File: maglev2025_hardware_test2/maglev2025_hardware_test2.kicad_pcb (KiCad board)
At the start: 4 copper layers, 100 x 100 mm, 106 parts, among them J1 SWD, J2 PWRIn, U1 RY8411, U10 INA240A1PW, U11 INA240A1PW, U12 INA240A1PW, U2 TMAG5170-Q1, U3 STM32G474RBTx, U4 RS3236, U5 AT8236, U6 AT8236, U7 AT8236, U8 AT8236, U9 INA240A1PW, Y1 25MHz

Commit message: finish test2 sche
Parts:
- added C54: 100n, Capacitor_SMD:C_0603_1608Metric, F.Cu at (-25.0, 69.7)
- added C55: 100n, Capacitor_SMD:C_0603_1608Metric, F.Cu at (-25.0, 72.2)
- added C56: 100n, Capacitor_SMD:C_0603_1608Metric, F.Cu at (-25.0, 74.7)
- added C57: 10n, Capacitor_SMD:C_0603_1608Metric, F.Cu at (-25.0, 77.2)
- added C58: 100u 16V, Capacitor_THT:CP_Radial_D6.3mm_P2.50mm, F.Cu at (-42.2, 72.3)
- added C59: 10u, Capacitor_SMD:C_1206_3216Metric, F.Cu at (-42.2, 100.8)
- added C60: 100n, Capacitor_SMD:C_0603_1608Metric, F.Cu at (-43.0, 85.4)
- added C61: 10n, Capacitor_SMD:C_0603_1608Metric, F.Cu at (-43.0, 87.9)
- added C62: 100u 16V, Capacitor_THT:CP_Radial_D6.3mm_P2.50mm, F.Cu at (-42.2, 80.2)
- added C63: 10u, Capacitor_SMD:C_1206_3216Metric, F.Cu at (-42.2, 104.2)
- added C64: 10u, Capacitor_SMD:C_1206_3216Metric, F.Cu at (-42.2, 107.5)
- added C65: 10u, Capacitor_SMD:C_0603_1608Metric, F.Cu at (-43.0, 90.4)
- added C66: 20p, Capacitor_SMD:C_0603_1608Metric, F.Cu at (-43.0, 92.9)
- added C67: 100n, Capacitor_SMD:C_0603_1608Metric, F.Cu at (-43.0, 95.4)
- added C68: 100n, Capacitor_SMD:C_0603_1608Metric, F.Cu at (-43.0, 97.9)
- added C69: 100n, Capacitor_SMD:C_0603_1608Metric, F.Cu at (-39.0, 85.4)
- added C70: 100n, Capacitor_SMD:C_0603_1608Metric, F.Cu at (-39.0, 87.9)
- added C71: 100n, Capacitor_SMD:C_0603_1608Metric, F.Cu at (-39.0, 90.4)
- added C72: 100n, Capacitor_SMD:C_0603_1608Metric, F.Cu at (-39.0, 92.9)
- added C73: 100n, Capacitor_SMD:C_0603_1608Metric, F.Cu at (-39.0, 95.4)
- added C74: 100n, Capacitor_SMD:C_0603_1608Metric, F.Cu at (-39.0, 97.9)
- added C75: 100n, Capacitor_SMD:C_0603_1608Metric, F.Cu at (-35.0, 85.4)
- added C76: 100n, Capacitor_SMD:C_0603_1608Metric, F.Cu at (-35.0, 87.9)
- added C77: 100n, Capacitor_SMD:C_0603_1608Metric, F.Cu at (-35.0, 90.4)
- added C78: 100n, Capacitor_SMD:C_0603_1608Metric, F.Cu at (-35.0, 92.9)
- added C79: 100n, Capacitor_SMD:C_0603_1608Metric, F.Cu at (-35.0, 95.4)
- added C80: 100n, Capacitor_SMD:C_0603_1608Metric, F.Cu at (-35.0, 97.9)
- added C81: 100n, Capacitor_SMD:C_0603_1608Metric, F.Cu at (-31.0, 85.4)
- added C82: 100n, Capacitor_SMD:C_0603_1608Metric, F.Cu at (-25.0, 79.7)
- added C83: 100n, Capacitor_SMD:C_0603_1608Metric, F.Cu at (-25.0, 82.2)
- added C84: 100n, Capacitor_SMD:C_0603_1608Metric, F.Cu at (-25.0, 84.7)
- added D10: WS2812B, LED_SMD:LED_WS2812B_PLCC4_5.0x5.0mm_P3.2mm, F.Cu at (-65.3, 98.2)
- added D11: DSS34, Diode_SMD:D_SMF, F.Cu at (-36.5, 107.5)
- added D12: WS2812B, LED_SMD:LED_WS2812B_PLCC4_5.0x5.0mm_P3.2mm, F.Cu at (-65.3, 104.8)
- added D13: WS2812B, LED_SMD:LED_WS2812B_PLCC4_5.0x5.0mm_P3.2mm, F.Cu at (-57.2, 71.7)
- added D14: WS2812B, LED_SMD:LED_WS2812B_PLCC4_5.0x5.0mm_P3.2mm, F.Cu at (-57.2, 78.3)
- added D15: WS2812B, LED_SMD:LED_WS2812B_PLCC4_5.0x5.0mm_P3.2mm, F.Cu at (-57.2, 85.0)
- added D16: WS2812B, LED_SMD:LED_WS2812B_PLCC4_5.0x5.0mm_P3.2mm, F.Cu at (-57.2, 91.6)
- added D17: WS2812B, LED_SMD:LED_WS2812B_PLCC4_5.0x5.0mm_P3.2mm, F.Cu at (-57.2, 98.2)
- added D18: WS2812B, LED_SMD:LED_WS2812B_PLCC4_5.0x5.0mm_P3.2mm, F.Cu at (-57.2, 104.8)
- added D19: WS2812B, LED_SMD:LED_WS2812B_PLCC4_5.0x5.0mm_P3.2mm, F.Cu at (-49.1, 71.7)
- added D20: WS2812B, LED_SMD:LED_WS2812B_PLCC4_5.0x5.0mm_P3.2mm, F.Cu at (-49.1, 78.3)
- added D21: WS2812B, LED_SMD:LED_WS2812B_PLCC4_5.0x5.0mm_P3.2mm, F.Cu at (-49.1, 85.0)
- added D29: LED, LED_SMD:LED_0603_1608Metric, F.Cu at (0.41, 69.7)
- added D30: LED, LED_SMD:LED_0603_1608Metric, F.Cu at (0.41, 72.3)
- added D31: LED, LED_SMD:LED_0603_1608Metric, F.Cu at (0.41, 74.9)
- added D4: DSS34, Diode_SMD:D_SMA, F.Cu at (-22.9, 95.7)
- added D6: WS2812B, LED_SMD:LED_WS2812B_PLCC4_5.0x5.0mm_P3.2mm, F.Cu at (-65.3, 71.7)
- added D7: WS2812B, LED_SMD:LED_WS2812B_PLCC4_5.0x5.0mm_P3.2mm, F.Cu at (-65.3, 78.3)
- added D8: WS2812B, LED_SMD:LED_WS2812B_PLCC4_5.0x5.0mm_P3.2mm, F.Cu at (-65.3, 85.0)
- added D9: WS2812B, LED_SMD:LED_WS2812B_PLCC4_5.0x5.0mm_P3.2mm, F.Cu at (-65.3, 91.6)
- added F3: 5A, Fuse:Fuse_1206_3216Metric, F.Cu at (-15.5, 90.1)
- added J3: Conn_01x04, Connector_PinHeader_2.54mm:PinHeader_1x04_P2.54mm_Vertical, F.Cu at (-8.62, 70.7)
- added J4: Conn_01x04_MountingPin, Connector_JST:JST_GH_BM04B-GHS-TBT_1x04-1MP_P1.25mm_Vertical, F.Cu at (-5.70, 95.0)
- added J5: USB_C_Receptacle_USB2.0, Connector_USB:USB_C_Receptacle_HRO_TYPE-C-31-M-12, F.Cu at (-5.09, 86.5)
- added J6: Conn_01x04, Connector_PinHeader_2.54mm:PinHeader_1x04_P2.54mm_Vertical, F.Cu at (-3.96, 70.7)
- added L6: 15u, Inductor_SMD:L_Sunlord_MWSA0402S, F.Cu at (-33.7, 71.3)
- added Q1: AO3400A, Package_TO_SOT_SMD:SOT-23, F.Cu at (-34.6, 81.4)
- added R21: 33r, Resistor_SMD:R_0603_1608Metric, F.Cu at (-25.0, 87.2)
- added R22: 33r, Resistor_SMD:R_0603_1608Metric, F.Cu at (-21.0, 69.7)
- added R23: 4.7k, Resistor_SMD:R_0603_1608Metric, F.Cu at (-21.0, 72.2)
- added R24: 4.7k, Resistor_SMD:R_0603_1608Metric, F.Cu at (-21.0, 74.7)
- added R25: 33r, Resistor_SMD:R_0603_1608Metric, F.Cu at (-21.0, 77.2)
- added R26: 33r, Resistor_SMD:R_0603_1608Metric, F.Cu at (-21.0, 79.7)
- added R27: 1M, Resistor_SMD:R_0603_1608Metric, F.Cu at (-21.0, 82.2)
- added R28: 33r, Resistor_SMD:R_0603_1608Metric, F.Cu at (-21.0, 84.7)
- added R29: 33r, Resistor_SMD:R_0603_1608Metric, F.Cu at (-21.0, 87.2)
- added R30: R_US, Resistor_SMD:R_2512_6332Metric, F.Cu at (-22.6, 90.9)
- added R31: 10k, Resistor_SMD:R_0603_1608Metric, F.Cu at (-17.0, 69.7)
- added R32: 1k, Resistor_SMD:R_0603_1608Metric, F.Cu at (-17.0, 72.2)
- added R33: 3.24k, Resistor_SMD:R_0603_1608Metric, F.Cu at (-31.0, 90.4)
- added R34: 10k, Resistor_SMD:R_0603_1608Metric, F.Cu at (-31.0, 92.9)
- added R35: 33r, Resistor_SMD:R_0603_1608Metric, F.Cu at (-31.0, 95.4)
- added R36: 33R, Resistor_SMD:R_0603_1608Metric, F.Cu at (-31.0, 97.9)
- added R37: 33r, Resistor_SMD:R_0603_1608Metric, F.Cu at (-17.0, 74.7)
- added R38: 33r, Resistor_SMD:R_0603_1608Metric, F.Cu at (-17.0, 77.2)
- added R39: 33r, Resistor_SMD:R_0603_1608Metric, F.Cu at (-17.0, 79.7)
- added R40: 33r, Resistor_SMD:R_0603_1608Metric, F.Cu at (-17.0, 82.2)
- added R41: 330, Resistor_SMD:R_0603_1608Metric, F.Cu at (-17.0, 84.7)
- added R42: 1k, Resistor_SMD:R_0603_1608Metric, F.Cu at (-17.0, 87.2)
- added R43: 10k, Resistor_SMD:R_0603_1608Metric, F.Cu at (-12.9, 69.7)
- added R44: 330, Resistor_SMD:R_0603_1608Metric, F.Cu at (-12.9, 72.2)
- added R45: 1k, Resistor_SMD:R_0603_1608Metric, F.Cu at (-12.9, 74.7)
- added R46: 10k, Resistor_SMD:R_0603_1608Metric, F.Cu at (-12.9, 77.2)
- added R47: 330, Resistor_SMD:R_0603_1608Metric, F.Cu at (-12.9, 79.7)
- added R48: 1k, Resistor_SMD:R_0603_1608Metric, F.Cu at (-12.9, 82.2)
- added R49: 10k, Resistor_SMD:R_0603_1608Metric, F.Cu at (-12.9, 84.7)
- added R6: 10k, Resistor_SMD:R_0603_1608Metric, F.Cu at (-31.0, 87.9)
- added RN4: 33x4, Resistor_SMD:R_Array_Convex_4x0603, F.Cu at (-35.0, 76.6)
- added U13: TPS5430DDA, Package_SO:TI_SO-PowerPAD-8_ThermalVias, F.Cu at (-35.1, 102.6)
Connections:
- C1 pad 1: VREF -> VREF_MCU
- C2 pad 1: VREF -> VREF_MCU
- R11 pad 1: GND -> GND_PWR
- R12 pad 1: GND -> GND_PWR
- R13 pad 1: GND -> GND_PWR
- R14 pad 1: GND -> GND_PWR
- R20 pad 1: Net-(U3-PA15) -> Net-(U3-PA13)
- R4 pad 1: Net-(U3-PB7) -> Net-(U3-PA3)
- U3 pad 10: unconnected-(U3-PC2-Pad10) -> ISENSE_D_MCU
- U3 pad 11: unconnected-(U3-PC3-Pad11) -> ISENSE_C_MCU
- U3 pad 12: unconnected-(U3-PA0-Pad12) -> ISENSE_B_MCU
- U3 pad 13: unconnected-(U3-PA1-Pad13) -> ISENSE_A_MCU
- U3 pad 17: unconnected-(U3-PA3-Pad17) -> Net-(U3-PA3)
- U3 pad 18: ISENSE_A_MCU -> Net-(RN4-R4.1)
- U3 pad 19: unconnected-(U3-PA5-Pad19) -> Net-(RN4-R3.1)
- U3 pad 2: unconnected-(U3-PC13-Pad2) -> /PC13
- U3 pad 20: ISENSE_B_MCU -> Net-(RN4-R2.1)
- U3 pad 21: unconnected-(U3-PA7-Pad21) -> Net-(RN4-R1.1)
- U3 pad 22: ISENSE_C_MCU -> /USART1_TX
- U3 pad 23: unconnected-(U3-PC5-Pad23) -> /USART1_RX
- U3 pad 24: unconnected-(U3-PB0-Pad24) -> VREF_MCU
- U3 pad 25: unconnected-(U3-PB1-Pad25) -> VREF
- U3 pad 26: ISENSE_D_MCU -> unconnected-(U3-PB2-Pad26)
- U3 pad 28: VREF -> VREF_MCU
- U3 pad 3: unconnected-(U3-PC14-Pad3) -> /PC14
- U3 pad 33: unconnected-(U3-PB11-Pad33) -> /OPAMP4_VINP
- U3 pad 4: unconnected-(U3-PC15-Pad4) -> /PC15
- U3 pad 40: unconnected-(U3-PC8-Pad40) -> I2C3_SCL
- U3 pad 41: unconnected-(U3-PC9-Pad41) -> I2C3_SDA
- U3 pad 49: unconnected-(U3-PA13-Pad49) -> Net-(U3-PA13)
- U3 pad 51: Net-(U3-PA15) -> unconnected-(U3-PA15-Pad51)
- U3 pad 52: unconnected-(U3-PC10-Pad52) -> /PC10
- U3 pad 53: unconnected-(U3-PC11-Pad53) -> /PC11
- U3 pad 54: unconnected-(U3-PC12-Pad54) -> /PC12
- U3 pad 55: unconnected-(U3-PD2-Pad55) -> /PD2
- U3 pad 56: Net-(RN2-R4.1) -> /PB3
- U3 pad 57: Net-(RN2-R3.1) -> /UCPD1_CC2
- U3 pad 58: Net-(RN2-R2.1) -> unconnected-(U3-PB5-Pad58)
- U3 pad 59: Net-(RN2-R1.1) -> /UCPD1_CC1
- U3 pad 60: Net-(U3-PB7) -> unconnected-(U3-PB7-Pad60)
- U3 pad 62: Net-(U3-PB9) -> unconnected-(U3-PB9-Pad62)
- U3 pad 8: unconnected-(U3-PC0-Pad8) -> BUZZER
- U3 pad 9: unconnected-(U3-PC1-Pad9) -> VSENSE_VBUS
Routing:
- net (no net): track 0.00 -> 40.3 mm, vias 0 -> 2
- net Net-(U3-PA15): track 34.8 -> 0.00 mm, vias 2 -> 0
- net Net-(U3-PB7): track 5.46 -> 0.00 mm

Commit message: start layout
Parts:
- removed C54, C56, C82, C83, C84: 100n, Capacitor_SMD:C_0603_1608Metric
- removed D29, D30, D31: LED, LED_SMD:LED_0603_1608Metric
- removed R11, R12, R13, R14: 100m, Resistor_SMD:R_2512_6332Metric
- removed R43, R46, R49: 10k, Resistor_SMD:R_0603_1608Metric
- removed R44, R47: 330, Resistor_SMD:R_0603_1608Metric
- removed R45, R48: 1k, Resistor_SMD:R_0603_1608Metric
- removed the R6 at (61.5, 127.5)
- removed RN2: 33x4, Resistor_SMD:R_Array_Convex_4x0603
- added BZ1: Buzzer, RM25:MLT-9032, F.Cu at (-13.6, 130.3)
- added C85: 100n, Capacitor_SMD:C_0603_1608Metric, F.Cu at (-40.8, 141.5)
- added C86: 100n, Capacitor_SMD:C_0603_1608Metric, F.Cu at (-40.8, 144.0)
- added C87: 100n, Capacitor_SMD:C_0603_1608Metric, F.Cu at (-40.8, 146.5)
- added C88: 100n, Capacitor_SMD:C_0603_1608Metric, F.Cu at (-40.8, 149.0)
- added D5: DSS34, Diode_SMD:D_SMA, F.Cu at (203.7, 138.8)
- added R50: 10k, Resistor_SMD:R_0603_1608Metric, F.Cu at (-36.8, 146.5)
- added R51: 33, Resistor_SMD:R_0603_1608Metric, F.Cu at (-36.8, 149.0)
- added R52: 10k, Resistor_SMD:R_0603_1608Metric, F.Cu at (-32.8, 141.5)
- added R53: 33, Resistor_SMD:R_0603_1608Metric, F.Cu at (-32.8, 144.0)
- added R54: 33, Resistor_SMD:R_0603_1608Metric, F.Cu at (-32.8, 146.5)
- added R55: 10k, Resistor_SMD:R_0603_1608Metric, F.Cu at (-32.8, 149.0)
- added SW4: RotaryEncoder_Switch_MP, Rotary_Encoder:RotaryEncoder_Alps_EC11E-Switch_Vertical_H20mm_MountingHoles, F.Cu at (-40.8, 130.1)
- D1: moved to B.Cu
- D4: value DSS34 -> DK5V45R10; footprint Diode_SMD:D_SMA -> Diode_SMD:D_PowerDI-5
- R41: value 330 -> 5.1k
- R42: value 1k -> 5.1k
- moved C63 219.8 mm to (177.6, 103.6)
- moved C64 219.8 mm to (177.6, 106.9)
- moved R33 219.8 mm to (188.8, 89.8)
- moved R6 219.8 mm to (188.8, 87.3)
- moved C62 215.8 mm to (170.2, 118.4), turned to 180 degrees
- moved C58 189.3 mm to (139.2, 126.5), turned to 180 degrees
- moved C61 186.7 mm to (142.3, 110.9), turned to -90 degrees
- moved C60 183.9 mm to (138.4, 115.5), turned to 180 degrees
- moved L6 183.5 mm to (145.5, 111.1), turned to 90 degrees
- moved C59 181.4 mm to (138.4, 117.5), turned to 180 degrees
- moved U13 174.0 mm to (138.7, 110.8), turned to -90 degrees
- moved RN4 117.5 mm to (71.0, 127.5), turned to 90 degrees
- moved R41 60.1 mm to (-36.8, 141.5)
- moved R42 60.1 mm to (-36.8, 144.0)
- moved D4 47.5 mm to (-26.4, 143.0)
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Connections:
- C55 pad 1: +3.3V -> +5V
- J4 pad 3: +3.3V -> +5V
- R41 pad 1: Net-(D29-K) -> GND
- R41 pad 2: /Connectivity/PC13 -> /Connectivity/UCPD1_CC1
- R42 pad 1: +3.3V -> GND
- R42 pad 2: Net-(D29-A) -> /Connectivity/UCPD1_CC2
- U3 pad 30: unconnected-(U3-PB10-Pad30) -> /PB10_ROTENC_BTN
- U3 pad 38: unconnected-(U3-PC6-Pad38) -> PC6_T8C1
- U3 pad 39: unconnected-(U3-PC7-Pad39) -> PC7_T8C2
- U5 pad 7: Net-(U5-ISEN) -> GND_PWR
- U6 pad 7: Net-(U6-ISEN) -> GND_PWR
- U7 pad 7: Net-(U7-ISEN) -> GND_PWR
- U8 pad 7: Net-(U8-ISEN) -> GND_PWR
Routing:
- net +3.3V: track 261.0 -> 141.6 mm, vias 16 -> 5
- net ISENSE_D: track 86.4 -> 1.10 mm, vias 2 -> 1
- net ISENSE_C: track 75.6 -> 1.24 mm, vias 2 -> 1
- net ISENSE_B: track 67.1 -> 1.34 mm, vias 2 -> 1
- net ISENSE_A: track 54.5 -> 1.45 mm, vias 2 -> 1
- net ~{MAG_ALRT}: track 51.8 -> 0.00 mm, vias 2 -> 0
- net CTRL_C2: track 56.8 -> 8.12 mm, vias 2 -> 1
- net CTRL_C1: track 57.2 -> 8.99 mm, vias 2 -> 1
- net SPI1_SCK: track 47.9 -> 0.00 mm
- net SPI1_MOSI: track 46.7 -> 0.00 mm
- net SPI1_MISO: track 45.2 -> 0.00 mm
- net ~{MAG_CS}: track 44.5 -> 0.00 mm, vias 2 -> 0
- net (no net): track 40.3 -> 0.00 mm, vias 2 -> 0
- net GND: track 52.2 -> 16.1 mm, vias 636 -> 216
- net Net-(U3-PA14): track 35.2 -> 0.00 mm, vias 2 -> 0
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
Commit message: addjust layout
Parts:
- removed C80: 100n, Capacitor_SMD:C_0603_1608Metric
- removed D21: WS2812B, LED_SMD:LED_WS2812B_PLCC4_5.0x5.0mm_P3.2mm
- BZ1, C57, C65, C66, C67, C68, C69, C70, C71, C72, C73, C74, C75, C76, C77, C78, C79, C81, C9, D10, D11, D12, D13, D14, D15, D16, D17, D18, D19, D20, D6, D7, D8, D9, F3, R1, R27, R28, R29, R36, R41, R42: moved to B.Cu
- moved D12 215.2 mm to (144.9, 150.5)
- moved D10 208.2 mm to (132.5, 163.0)
- moved D14 202.3 mm to (144.9, 85.5)
- moved D13 194.1 mm to (132.5, 113.0)
- moved D15 190.1 mm to (132.5, 73.0)
- moved D9 189.3 mm to (110.0, 163.0)
- moved C79 187.6 mm to (143.2, 154.0)
- moved C74 179.9 mm to (128.2, 164.2), turned to 90 degrees
- moved D8 173.8 mm to (90.0, 163.0)
- moved D16 173.2 mm to (115.0, 73.0)
- moved C81 171.6 mm to (140.6, 86.6), turned to 90 degrees
- moved C76 165.3 mm to (128.2, 114.0), turned to 90 degrees
- moved C75 163.6 mm to (128.2, 74.2), turned to 90 degrees
- moved C73 160.2 mm to (105.6, 164.4), turned to 90 degrees
- moved D7 157.5 mm to (67.5, 163.0)
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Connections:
- C85 pad 2: /Connectivity/PB10_ROTENC_BTN -> /PB10_ROTENC_BTN
- D20 pad 2: Net-(D20-DOUT) -> unconnected-(D20-DOUT-Pad2)
- R21 pad 1: /Connectivity/USART1_TX -> /USART1_RX
- R26 pad 1: /Connectivity/USART1_RX -> /USART1_TX
- R28 pad 2: /Connectivity/UCPD1_CC1 -> /UCPD1_CC1
- R29 pad 2: /Connectivity/UCPD1_CC2 -> /UCPD1_CC2
- R37 pad 1: /Connectivity/PD2 -> /PD2
- R38 pad 1: /Connectivity/PC10 -> /PC10
- R39 pad 1: /Connectivity/PC11 -> /PC11
- R40 pad 1: /Connectivity/PC12 -> /PC12
- R41 pad 2: /Connectivity/UCPD1_CC1 -> /UCPD1_CC1
- R42 pad 2: /Connectivity/UCPD1_CC2 -> /UCPD1_CC2
- R51 pad 1: /Connectivity/PB10_ROTENC_BTN -> /PB10_ROTENC_BTN
- U3 pad 33: /OPAMP4_VINP -> GND_PWR
- U5 pad 1: GND -> GND_PWR
- U5 pad 9: GND -> GND_PWR
- U6 pad 1: GND -> GND_PWR
- U6 pad 9: GND -> GND_PWR
- U7 pad 1: GND -> GND_PWR
- U7 pad 9: GND -> GND_PWR
- U8 pad 1: GND -> GND_PWR
- U8 pad 9: GND -> GND_PWR
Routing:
- net +3.3V: track 141.6 -> 0.00 mm, vias 5 -> 0
- net VREF: track 76.4 -> 0.00 mm, vias 12 -> 0
- net VPP: track 68.1 -> 0.00 mm
- net CTRL_D1: track 54.7 -> 0.00 mm, vias 1 -> 0
- net CTRL_D2: track 53.5 -> 0.00 mm, vias 1 -> 0
- net /USART1_TX: track 0.00 -> 51.8 mm
- net /USART1_RX: track 0.00 -> 50.7 mm
- net ~{MAG_ALRT}: track 0.00 -> 41.6 mm
- net SPI1_SCK: track 0.00 -> 41.6 mm
- net SPI1_MOSI: track 0.00 -> 41.6 mm
- net SPI1_MISO: track 0.00 -> 39.1 mm
- net ~{MAG_CS}: track 0.00 -> 37.2 mm, vias 0 -> 2
- net CTRL_B1: track 29.7 -> 0.00 mm, vias 1 -> 0
- net CTRL_B2: track 29.3 -> 0.00 mm, vias 1 -> 0
- net GND_PWR: track 23.8 -> 0.00 mm
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- removed copper zone on F.Cu, net +3.3V
- removed copper zone on F.Cu, net /5V
- removed copper zone on B.Cu, net GND
- removed copper zone on F.Cu, net GND
- removed copper zone on In1.Cu, net GND
- removed copper zone on In2.Cu, net GND
- removed copper zone on F.Cu, net Net-(D2-A1)
- removed copper zone on F.Cu, net Net-(L2-+)
- removed copper zone on F.Cu, net Net-(L3-+)
- removed copper zone on F.Cu, net Net-(L4-+)
- removed copper zone on F.Cu, net Net-(L5-+)
- removed copper zone on F.Cu, net Net-(U1-BS)
- removed copper zone on F.Cu, net Net-(U1-LX)
- removed copper zone on F.Cu, net Net-(U10--)
- removed copper zone on F.Cu, net Net-(U11--)
- removed copper zone on F.Cu, net Net-(U12--)
- removed copper zone on F.Cu, net Net-(U5-OUT2)
- removed copper zone on F.Cu, net VPP
- removed copper zone on F.Cu, net VREF
- removed copper zone on In2.Cu, net VREF

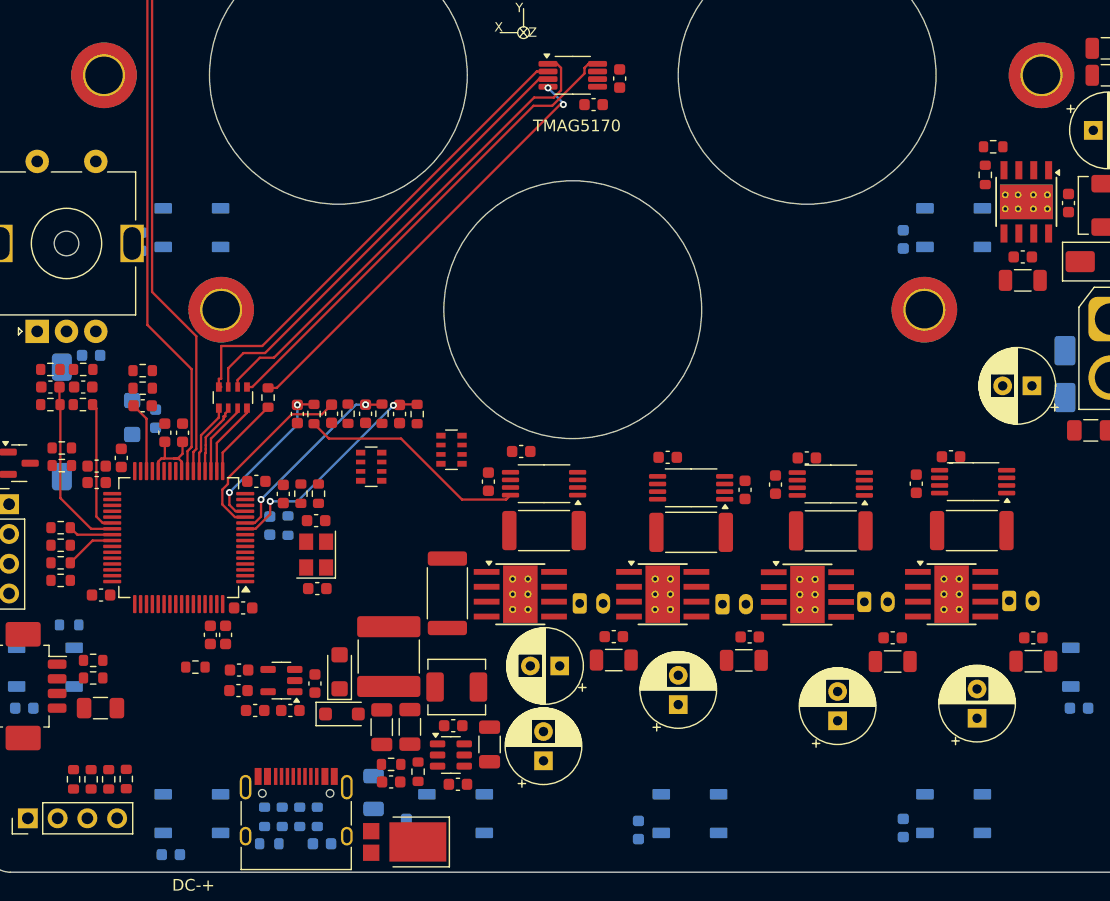
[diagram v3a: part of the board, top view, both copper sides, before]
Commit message: change adc pin out
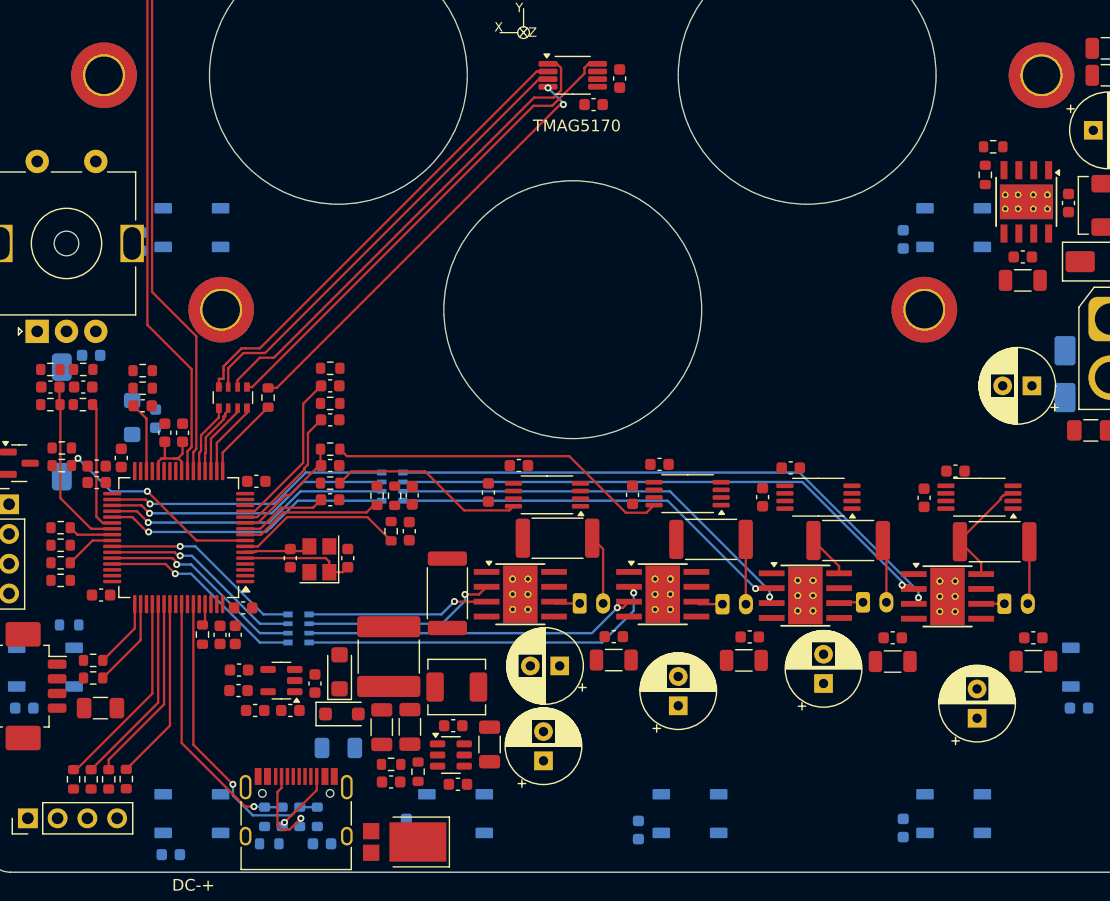
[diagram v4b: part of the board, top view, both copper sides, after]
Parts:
- C9, R1: moved to F.Cu
- RN1, RN3: moved to B.Cu
- moved RN1 15.1 mm to (76.6, 147.2)
- moved R17 14.0 mm to (136.0, 139.8)
- moved C46 13.7 mm to (118.6, 133.5)
- moved U12 13.3 mm to (121.0, 136.0)
- moved C50 13.2 mm to (116.2, 136.0)
- moved C45 12.7 mm to (132.7, 133.8)
- moved C49 12.7 mm to (130.0, 136.1)
- moved U11 12.7 mm to (134.7, 136.0)
- moved L5 12.5 mm to (124.8, 145.0)
- moved U8 12.5 mm to (119.8, 144.4)
- moved L4 12.0 mm to (136.8, 145.1)
- moved U7 12.0 mm to (132.0, 144.5)
- moved C9 11.9 mm to (86.0, 138.9)
- moved C88 11.0 mm to (86.3, 135.8), turned to 90 degrees
- moved R18 10.6 mm to (123.5, 139.7)
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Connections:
- U3 pad 10: ISENSE_D_MCU -> ISENSE_A_MCU
- U3 pad 11: ISENSE_C_MCU -> ISENSE_B_MCU
- U3 pad 12: ISENSE_B_MCU -> ISENSE_C_MCU
- U3 pad 13: ISENSE_A_MCU -> ISENSE_D_MCU
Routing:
- net CTRL_C1: track 0.00 -> 49.4 mm, vias 0 -> 1
- net CTRL_C2: track 0.00 -> 47.5 mm, vias 0 -> 1
- net CTRL_D1: track 0.00 -> 35.3 mm, vias 0 -> 1
- net CTRL_D2: track 0.00 -> 34.6 mm, vias 0 -> 1
- net CTRL_B2: track 0.00 -> 31.0 mm, vias 0 -> 1
- net ISENSE_B: track 0.00 -> 29.3 mm
- net CTRL_B1: track 0.00 -> 28.4 mm, vias 0 -> 1
- net /UCPD1_CC1: track 0.00 -> 25.9 mm, vias 0 -> 1
- net /MCU_D2: track 0.00 -> 24.6 mm, vias 0 -> 1
- net /MCU_D1: track 0.00 -> 24.5 mm, vias 0 -> 1
- net /MCU_C2: track 0.00 -> 24.4 mm, vias 0 -> 1
- net /MCU_C1: track 0.00 -> 24.3 mm, vias 0 -> 1
- net /UCPD1_CC2: track 0.00 -> 22.7 mm, vias 0 -> 1
- net BUZZER: track 0.00 -> 18.0 mm, vias 0 -> 2
- net /MCU_B2: track 0.00 -> 17.8 mm, vias 0 -> 1
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
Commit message: finish wiring
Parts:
- moved C73 9.08 mm to (114.3, 161.8), turned to -90 degrees
- moved C74 8.84 mm to (136.7, 161.8), turned to -90 degrees
- moved C31 8.68 mm to (100.8, 158.8)
- moved C68 8.06 mm to (57.0, 82.0), turned to 180 degrees
- moved C70 8.02 mm to (87.1, 69.5), turned to 180 degrees
- moved C77 8.01 mm to (69.6, 159.5), turned to 180 degrees
- moved C69 7.96 mm to (117.0, 69.4), turned to 180 degrees
- moved C75 7.96 mm to (134.6, 69.5), turned to 180 degrees
- moved C67 7.94 mm to (69.5, 69.4), turned to 180 degrees
- moved C33 7.89 mm to (125.1, 158.8), turned to 180 degrees
- moved C76 7.88 mm to (134.6, 109.4), turned to 0 degrees
- moved C81 7.88 mm to (147.0, 82.0), turned to 180 degrees
- moved C71 7.86 mm to (69.5, 109.5), turned to 180 degrees
- moved C78 7.80 mm to (92.0, 159.5), turned to 180 degrees
- moved C5 7.11 mm to (94.8, 165.1)
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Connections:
- C27 pad 2: GND -> GND_PWR
- C28 pad 2: GND -> GND_PWR
- C29 pad 2: GND -> GND_PWR
- C30 pad 2: GND -> GND_PWR
- C31 pad 2: GND -> GND_PWR
- C32 pad 2: GND -> GND_PWR
- C33 pad 2: GND -> GND_PWR
- C34 pad 2: GND -> GND_PWR
- C39 pad 2: GND -> GND_PWR
- C40 pad 2: GND -> GND_PWR
- C41 pad 2: GND -> GND_PWR
- C42 pad 2: GND -> GND_PWR
- R37 pad 2: Net-(J6-Pin_1) -> Net-(J6-Pin_4)
- R38 pad 2: Net-(J6-Pin_2) -> Net-(J6-Pin_1)
- R39 pad 2: Net-(J6-Pin_3) -> Net-(J6-Pin_2)
- R40 pad 2: Net-(J6-Pin_4) -> Net-(J6-Pin_3)
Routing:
- net Net-(D16-DOUT): track 0.00 -> 60.4 mm
- net ISENSE_C: track 0.00 -> 59.5 mm
- net ISENSE_D: track 0.00 -> 53.5 mm
- net Net-(D12-DOUT): track 0.00 -> 53.0 mm
- net GND_PWR: track 0.00 -> 40.9 mm, vias 0 -> 2
- net Net-(D13-DOUT): track 0.00 -> 36.0 mm
- net Net-(D19-DOUT): track 0.00 -> 27.3 mm
- net Net-(D17-DOUT): track 0.00 -> 26.0 mm
- net Net-(D15-DOUT): track 0.00 -> 25.3 mm
- net Net-(D14-DOUT): track 0.00 -> 25.0 mm
- net Net-(D7-DOUT): track 0.00 -> 22.0 mm
- net Net-(R50-Pad2): track 0.00 -> 21.3 mm
- net Net-(D18-DOUT): track 0.00 -> 21.2 mm
- net Net-(R52-Pad2): track 0.00 -> 20.0 mm
- net Net-(D10-DIN): track 0.00 -> 19.0 mm
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- added copper zone on F.Cu, net +5V_BLINK
- added copper zone on F.Cu, net /5V
- added copper zone on In2.Cu, net /5V
- added copper zone on B.Cu, net GND_PWR
- added copper zone on F.Cu, net GND_PWR
- added copper zone on In1.Cu, net GND_PWR
- added copper zone on B.Cu, net Net-(BZ1--)
- added copper zone on F.Cu, net Net-(BZ1--)
- added copper zone on F.Cu, net Net-(D2-A1)
- added copper zone on B.Cu, net Net-(D4-A)
- added copper zone on F.Cu, net Net-(D4-A)
- added copper zone on F.Cu, net Net-(D5-K)
- added copper zone on B.Cu, net Net-(F3-Pad1)
- added copper zone on F.Cu, net Net-(F3-Pad1)
- added copper zone on F.Cu, net Net-(J2-Pin_2)
- added copper zone on F.Cu, net Net-(U1-LX)
- added copper zone on F.Cu, net Net-(U10--)
- added copper zone on F.Cu, net Net-(U11--)
- added copper zone on F.Cu, net Net-(U12--)
- added copper zone on F.Cu, net Net-(U5-OUT2)
- added copper zone on F.Cu, net VPP
